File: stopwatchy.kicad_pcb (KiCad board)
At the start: 2 copper layers, 70 x 97 mm, 62 parts, among them J2 RST_SOCKET, J4 PROG, Q1 SI2323DS-T1-E3, SW2 PWR_SW, SW3 BOOT_BTN, SW4 BTN_3, SW5 BTN_1, SW6 BTN_2, SW7 BTN_4, U1 AP2007SPER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

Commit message: updated adc_in route from switch and changed R1 from 560k to 56k
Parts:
- removed REF**: HS-HS24CG003-ARX-LCD, stopwatchy_library:HS-HS24CG003-ARX-LCD
- R3: value 560k -> 56k
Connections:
- BT1 pad 1: ADC_IN0 -> Net-(BT1-+)
- Q1 pad 3: ADC_IN0 -> Net-(BT1-+)
- R9 pad 1: Net-(SW2-B) -> ADC_IN0
- SW2 pad 1: ADC_IN0 -> Net-(BT1-+)
- SW2 pad 2: Net-(SW2-B) -> ADC_IN0
- U1 pad 4: Net-(SW2-B) -> ADC_IN0
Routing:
- net Net-(SW2-B): track 55.1 -> 0.00 mm, vias 1 -> 0
- net Net-(BT1-+): track 0.00 -> 47.2 mm, vias 0 -> 1
- net ADC_IN0: track 98.4 -> 100.6 mm, vias 3 -> 2
- net GND: vias 272 -> 271
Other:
- board text added: "STM32 Pocket Console"
- board text removed: "STM32 Handheld"

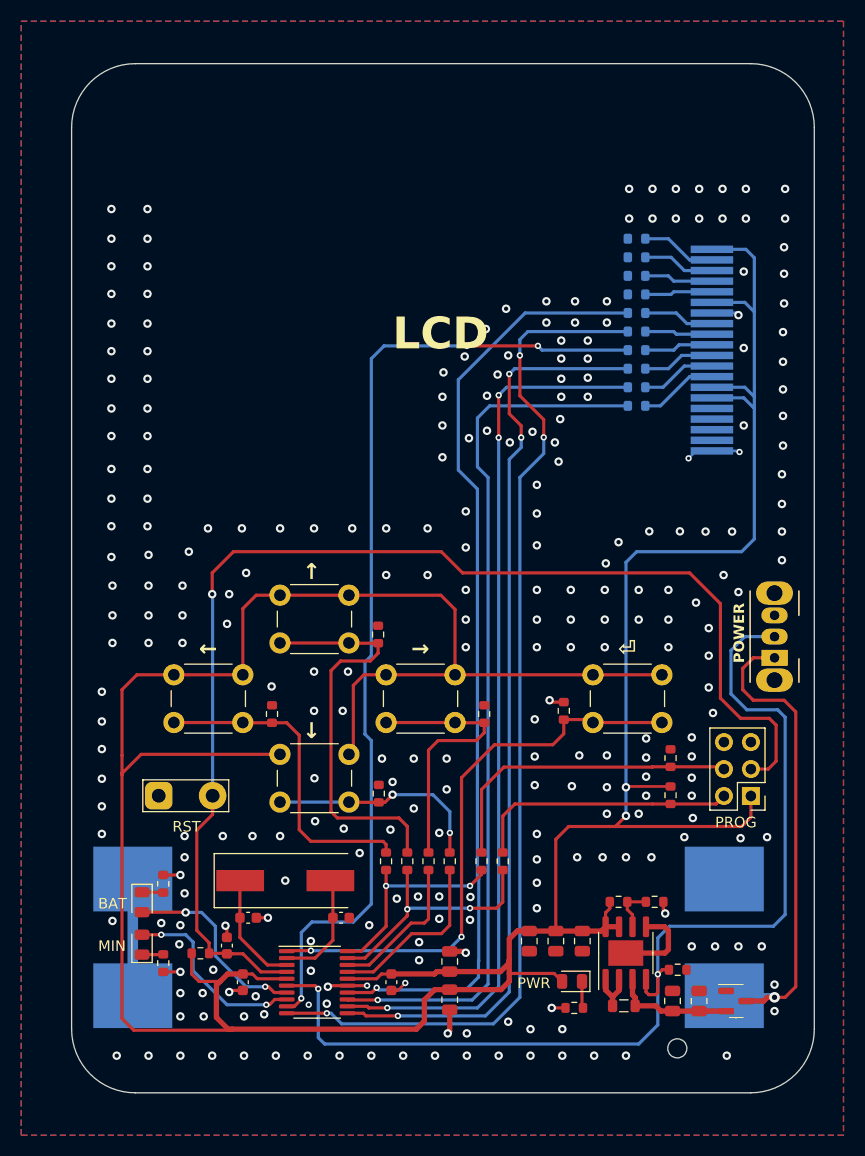
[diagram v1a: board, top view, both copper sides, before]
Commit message: removed unneeded resistors, fixed lcd connector placement, removed vias
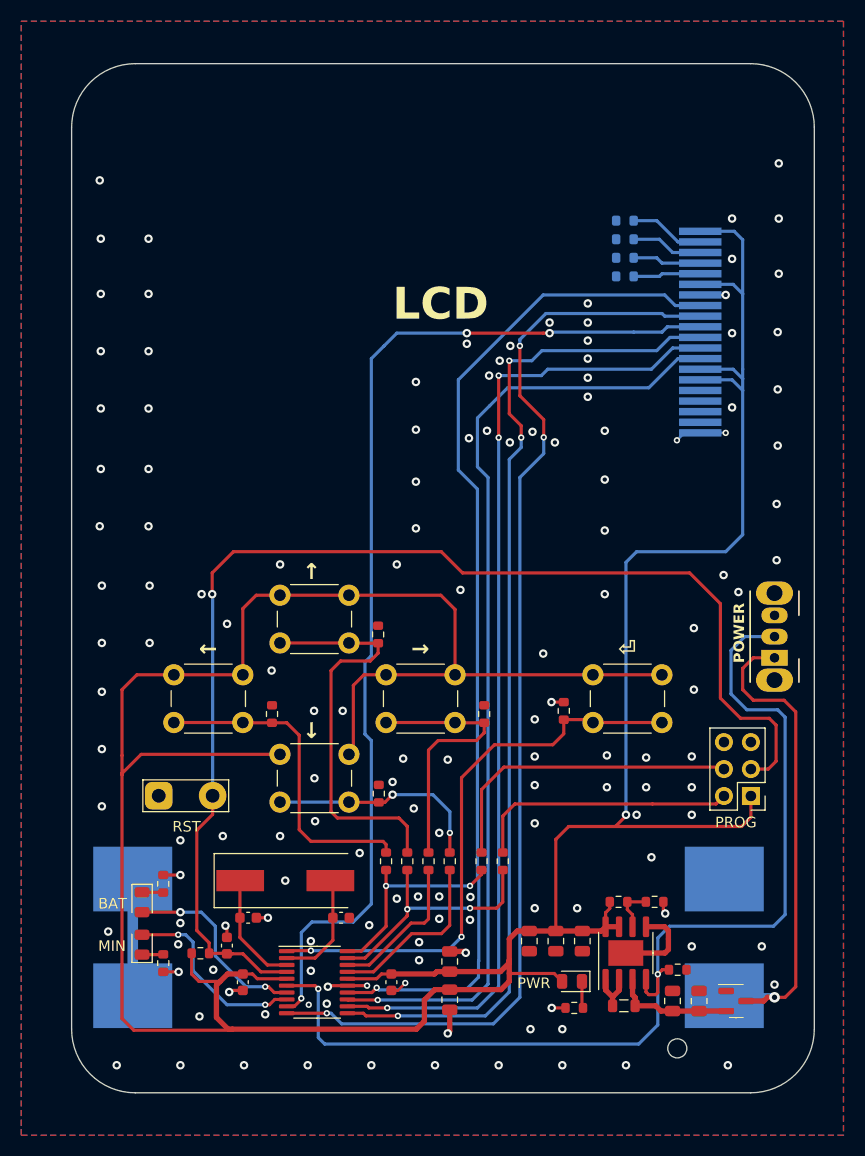
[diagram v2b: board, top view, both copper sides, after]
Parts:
- removed R19, R20: 10k, Resistor_SMD:R_0603_1608Metric
- removed R22, R23, R24, R25, R26, R27: 0, Resistor_SMD:R_0603_1608Metric
- moved R14 2.02 mm to (156.9, 38.8)
- moved R28 2.02 mm to (156.9, 40.5)
- moved R29 2.02 mm to (156.9, 42.3)
- moved R30 2.02 mm to (156.9, 44.0)
- moved U3 2.02 mm to (164.0, 48.8)
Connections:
- U3 pad 10: Net-(U3-SCLK) -> SPI1_SCK
- U3 pad 11: Net-(U3-D/C) -> ~{D/C}
- U3 pad 12: Net-(U3-/CS) -> SPI1_NSS
- U3 pad 13: Net-(U3-/RES) -> ~{RES}
- U3 pad 8: Net-(U3-MOSI) -> SPI1_MOSI
- U3 pad 9: Net-(U3-MISO) -> SPI1_MISO
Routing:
- net SPI1_MISO: track 83.4 -> 92.8 mm
- net SPI1_SCK: track 86.9 -> 95.6 mm
- net SPI1_MOSI: track 82.3 -> 91.0 mm
- net ~{RES}: track 88.8 -> 96.8 mm
- net SPI1_NSS: track 97.8 -> 105.4 mm
- net Net-(U3-MOSI): track 7.41 -> 0.00 mm
- net ~{D/C}: track 92.4 -> 99.8 mm
- net Net-(U3-MISO): track 7.10 -> 0.00 mm
- net Net-(U3-SCLK): track 6.79 -> 0.00 mm
- net Net-(U3-/RES): track 6.69 -> 0.00 mm
- net Net-(U3-D/C): track 6.48 -> 0.00 mm
- net Net-(U3-/CS): track 6.38 -> 0.00 mm
- net +3V3: track 340.8 -> 336.9 mm, vias 2 -> 1
- net GND: track 35.8 -> 35.0 mm, vias 271 -> 146
